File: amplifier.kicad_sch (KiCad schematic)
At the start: 20 parts, among them U5 PAM8403D

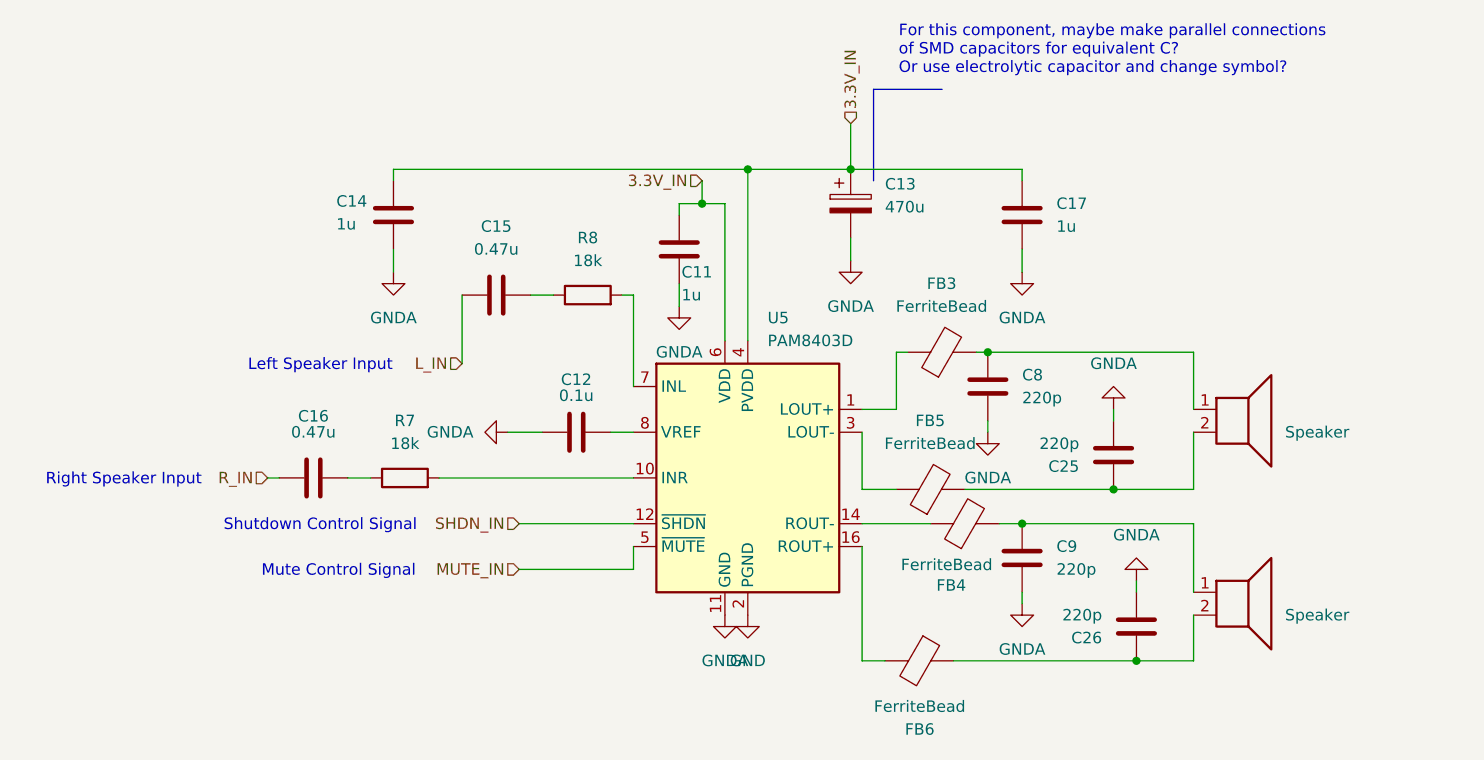
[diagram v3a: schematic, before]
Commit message: Changed grounds and began with new planes
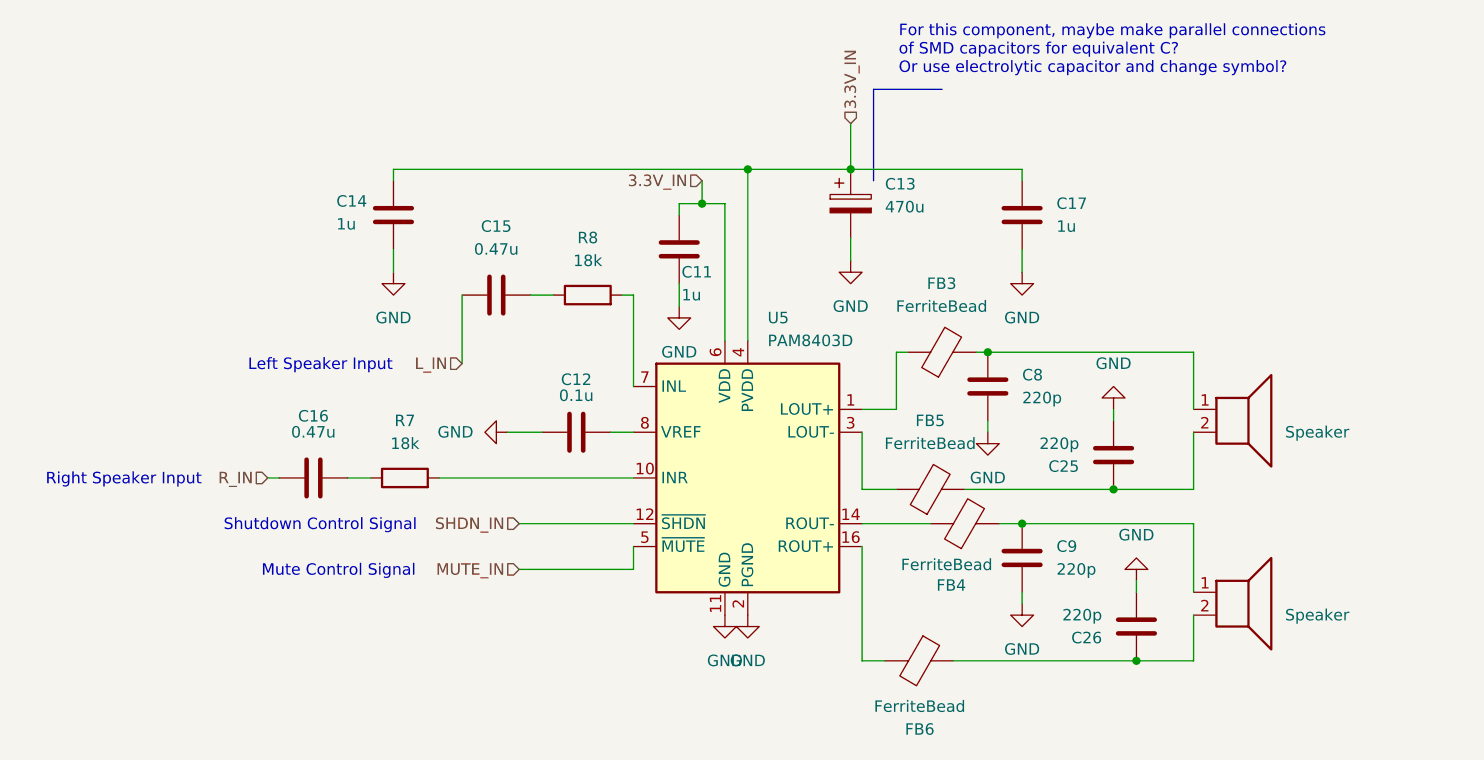
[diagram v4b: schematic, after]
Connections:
- net GNDA is gone; now on net GND: C11.2, C12.1, C13.2, C14.2, C17.2, C25.2, C26.2, C8.2, C9.2, U5.11 (GND)
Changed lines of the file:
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@@
 	)
 	(symbol
-		(lib_id "power:GNDA")
+		(lib_id "power:GND")
 		(at 165.1 106.68 0)
 		(unit 1)
@@
 		(dnp no)
 		(fields_autoplaced yes)
-		(property "Reference" "#PWR034"
+		(property "Reference" "#PWR34"
 			(at 165.1 113.03 0)
 			(effects
@@
 			)
 		)
-		(property "Value" "GNDA"
+		(property "Value" "GND"
 			(at 165.1 111.76 0)
 			(effects
@@
 			)
 		)
-		(property "Description" "Power symbol creates a global label with name \"GNDA\" , analog ground"
+		(property "Description" "Power symbol creates a global label with name \"GND\" , ground"
 			(at 165.1 106.68 0)
 			(effects
@@
 			(project "plant caretaker"
 				(path "/23b35dcc-615e-4aec-abee-c26cc3d8b906/64bd70cc-1431-45fc-8946-041e9631b1bb"
-					(reference "#PWR034")
+					(reference "#PWR34")
 					(unit 1)
 				)
@@
 	)
 	(symbol
-		(lib_id "power:GNDA")
+		(lib_id "power:GND")
 		(at 165.1 69.85 0)
 		(unit 1)
@@
 		(dnp no)
 		(fields_autoplaced yes)
-		(property "Reference" "#PWR033"
+		(property "Reference" "#PWR33"
 			(at 165.1 76.2 0)
 			(effects
@@
 			)
 		)
-		(property "Value" "GNDA"
+		(property "Value" "GND"
 			(at 165.1 74.93 0)
 			(effects
@@
 			)
 		)
-		(property "Description" "Power symbol creates a global label with name \"GNDA\" , analog ground"
+		(property "Description" "Power symbol creates a global label with name \"GND\" , ground"
 			(at 165.1 69.85 0)
 			(effects
@@
 			(project "plant caretaker"
 				(path "/23b35dcc-615e-4aec-abee-c26cc3d8b906/64bd70cc-1431-45fc-8946-041e9631b1bb"
-					(reference "#PWR033")
+					(reference "#PWR33")
 					(unit 1)
 				)
@@
 		(dnp no)
 		(fields_autoplaced yes)
-		(property "Reference" "#PWR011"
+		(property "Reference" "#PWR11"
 			(at 134.62 114.3 0)
 			(effects
@@
 			(project "plant caretaker"
 				(path "/23b35dcc-615e-4aec-abee-c26cc3d8b906/64bd70cc-1431-45fc-8946-041e9631b1bb"
-					(reference "#PWR011")
+					(reference "#PWR11")
 					(unit 1)
 				)
@@
 	)
 	(symbol
-		(lib_id "power:GNDA")
+		(lib_id "power:GND")
 		(at 161.29 87.63 0)
 		(unit 1)
@@
 		(dnp no)
 		(fields_autoplaced yes)
-		(property "Reference" "#PWR035"
+		(property "Reference" "#PWR35"
 			(at 161.29 93.98 0)
 			(effects
@@
 			)
 		)
-		(property "Value" "GNDA"
+		(property "Value" "GND"
 			(at 161.29 92.71 0)
 			(effects
@@
 			)
 		)
-		(property "Description" "Power symbol creates a global label with name \"GNDA\" , analog ground"
+		(property "Description" "Power symbol creates a global label with name \"GND\" , ground"
 			(at 161.29 87.63 0)
 			(effects
@@
 			(project "plant caretaker"
 				(path "/23b35dcc-615e-4aec-abee-c26cc3d8b906/64bd70cc-1431-45fc-8946-041e9631b1bb"
-					(reference "#PWR035")
+					(reference "#PWR35")
 					(unit 1)
 				)
@@
 	)
 	(symbol
-		(lib_id "power:GNDA")
+		(lib_id "power:GND")
 		(at 95.25 69.85 0)
 		(unit 1)
@@
 		(dnp no)
 		(fields_autoplaced yes)
-		(property "Reference" "#PWR012"
+		(property "Reference" "#PWR12"
 			(at 95.25 76.2 0)
 			(effects
@@
 			)
 		)
-		(property "Value" "GNDA"
+		(property "Value" "GND"
 			(at 95.25 74.93 0)
 			(effects
@@
 			)
 		)
-		(property "Description" "Power symbol creates a global label with name \"GNDA\" , analog ground"
+		(property "Description" "Power symbol creates a global label with name \"GND\" , ground"
 			(at 95.25 69.85 0)
 			(effects
@@
 			(project "plant caretaker"
 				(path "/23b35dcc-615e-4aec-abee-c26cc3d8b906/64bd70cc-1431-45fc-8946-041e9631b1bb"
-					(reference "#PWR012")
-					(unit 1)
-				)
-			)
-		)
-	)
-	(symbol
-		(lib_id "power:GNDA")
+					(reference "#PWR12")
+					(unit 1)
+				)
+			)
+		)
+	)
+	(symbol
+		(lib_id "power:GND")
 		(at 175.26 85.09 180)
 		(unit 1)
@@
 		(dnp no)
 		(fields_autoplaced yes)
-		(property "Reference" "#PWR038"
+		(property "Reference" "#PWR38"
 			(at 175.26 78.74 0)
 			(effects
@@
 			)
 		)
-		(property "Value" "GNDA"
+		(property "Value" "GND"
 			(at 175.26 80.01 0)
 			(effects
@@
 			)
 		)
-		(property "Description" "Power symbol creates a global label with name \"GNDA\" , analog ground"
+		(property "Description" "Power symbol creates a global label with name \"GND\" , ground"
 			(at 175.26 85.09 0)
 			(effects
@@
 			(project "plant caretaker"
 				(path "/23b35dcc-615e-4aec-abee-c26cc3d8b906/64bd70cc-1431-45fc-8946-041e9631b1bb"
-					(reference "#PWR038")
+					(reference "#PWR38")
 					(unit 1)
 				)
@@
 	)
 	(symbol
-		(lib_id "power:GNDA")
+		(lib_id "power:GND")
 		(at 107.95 87.63 270)
 		(unit 1)
@@
 		(dnp no)
 		(fields_autoplaced yes)
-		(property "Reference" "#PWR013"
+		(property "Reference" "#PWR13"
 			(at 101.6 87.63 0)
 			(effects
@@
 			)
 		)
-		(property "Value" "GNDA"
+		(property "Value" "GND"
 			(at 104.14 87.6299 90)
 			(effects
@@
 			)
 		)
-		(property "Description" "Power symbol creates a global label with name \"GNDA\" , analog ground"
+		(property "Description" "Power symbol creates a global label with name \"GND\" , ground"
 			(at 107.95 87.63 0)
 			(effects
@@
 			(project "plant caretaker"
 				(path "/23b35dcc-615e-4aec-abee-c26cc3d8b906/64bd70cc-1431-45fc-8946-041e9631b1bb"
-					(reference "#PWR013")
-					(unit 1)
-				)
-			)
-		)
-	)
-	(symbol
-		(lib_id "power:GNDA")
+					(reference "#PWR13")
+					(unit 1)
+				)
+			)
+		)
+	)
+	(symbol
+		(lib_id "power:GND")
 		(at 127 73.66 0)
 		(unit 1)
@@
 		(dnp no)
 		(fields_autoplaced yes)
-		(property "Reference" "#PWR014"
+		(property "Reference" "#PWR14"
 			(at 127 80.01 0)
 			(effects
@@
 			)
 		)
-		(property "Value" "GNDA"
+		(property "Value" "GND"
 			(at 127 78.74 0)
 			(effects
@@
 			)
 		)
-		(property "Description" "Power symbol creates a global label with name \"GNDA\" , analog ground"
+		(property "Description" "Power symbol creates a global label with name \"GND\" , ground"
 			(at 127 73.66 0)
 			(effects
@@
 			(project "plant caretaker"
 				(path "/23b35dcc-615e-4aec-abee-c26cc3d8b906/64bd70cc-1431-45fc-8946-041e9631b1bb"
-					(reference "#PWR014")
+					(reference "#PWR14")
 					(unit 1)
 				)
@@
 	)
 	(symbol
-		(lib_id "power:GNDA")
+		(lib_id "power:GND")
 		(at 177.8 104.14 180)
 		(unit 1)
@@
 		(dnp no)
 		(fields_autoplaced yes)
-		(property "Reference" "#PWR041"
+		(property "Reference" "#PWR41"
 			(at 177.8 97.79 0)
 			(effects
@@
 			)
 		)
-		(property "Value" "GNDA"
+		(property "Value" "GND"
 			(at 177.8 99.06 0)
 			(effects
@@
 			)
 		)
-		(property "Description" "Power symbol creates a global label with name \"GNDA\" , analog ground"
+		(property "Description" "Power symbol creates a global label with name \"GND\" , ground"
 			(at 177.8 104.14 0)
 			(effects
@@
 			(project "plant caretaker"
 				(path "/23b35dcc-615e-4aec-abee-c26cc3d8b906/64bd70cc-1431-45fc-8946-041e9631b1bb"
-					(reference "#PWR041")
+					(reference "#PWR41")
 					(unit 1)
 				)
@@
 	)
 	(symbol
-		(lib_id "power:GNDA")
+		(lib_id "power:GND")
 		(at 132.08 107.95 0)
 		(unit 1)
@@
 		(dnp no)
 		(fields_autoplaced yes)
-		(property "Reference" "#PWR015"
+		(property "Reference" "#PWR15"
 			(at 132.08 114.3 0)
 			(effects
@@
 			)
 		)
-		(property "Value" "GNDA"
+		(property "Value" "GND"
 			(at 132.08 113.03 0)
 			(effects
@@
 			)
 		)
-		(property "Description" "Power symbol creates a global label with name \"GNDA\" , analog ground"
+		(property "Description" "Power symbol creates a global label with name \"GND\" , ground"
 			(at 132.08 107.95 0)
 			(effects
@@
 			(project "plant caretaker"
 				(path "/23b35dcc-615e-4aec-abee-c26cc3d8b906/64bd70cc-1431-45fc-8946-041e9631b1bb"
-					(reference "#PWR015")
+					(reference "#PWR15")
 					(unit 1)
 				)
@@
 	)
 	(symbol
-		(lib_id "power:GNDA")
+		(lib_id "power:GND")
 		(at 146.05 68.58 0)
 		(unit 1)
@@
 		(dnp no)
 		(fields_autoplaced yes)
-		(property "Reference" "#PWR09"
+		(property "Reference" "#PWR9"
 			(at 146.05 74.93 0)
 			(effects
@@
 			)
 		)
-		(property "Value" "GNDA"
+		(property "Value" "GND"
 			(at 146.05 73.66 0)
 			(effects
@@
 			)
 		)
-		(property "Description" "Power symbol creates a global label with name \"GNDA\" , analog ground"
+		(property "Description" "Power symbol creates a global label with name \"GND\" , ground"
 			(at 146.05 68.58 0)
 			(effects
@@
 			(project "plant caretaker"
 				(path "/23b35dcc-615e-4aec-abee-c26cc3d8b906/64bd70cc-1431-45fc-8946-041e9631b1bb"
-					(reference "#PWR09")
-					(unit 1)
-				)
+					(reference "#PWR9")
+					(unit 1)
+				)

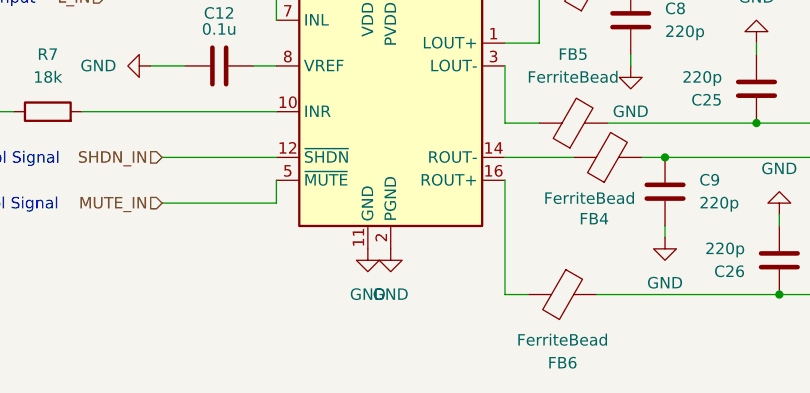
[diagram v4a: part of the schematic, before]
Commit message: Finished with ground planes and made board smaller
WARNING: Unconnected "ground power" for audio amplifier

Also fixed the ESP32 footprint on board only
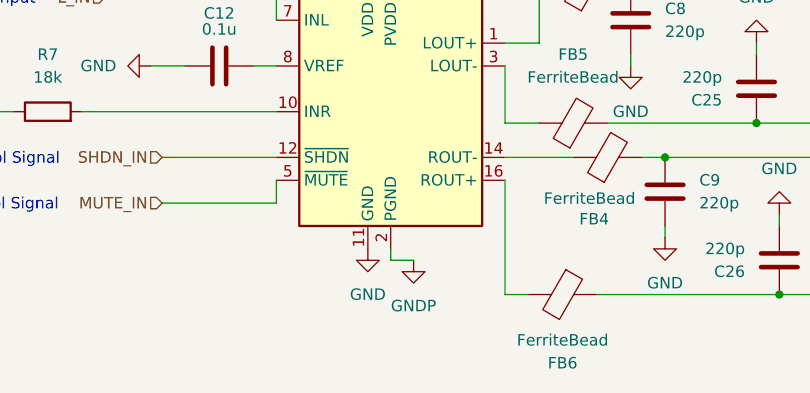
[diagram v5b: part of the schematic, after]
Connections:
- net GND: no longer U5.15 (PGND), U5.2 (PGND)
- new net GNDP: U5.15 (PGND), U5.2 (PGND)
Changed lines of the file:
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@@
+	(wire
+		(pts
+			(xy 134.62 109.22) (xy 134.62 107.95)
+		)
+		(stroke
+			(width 0)
+			(type default)
+		)
+	)
 	(wire
 		(pts
@@
 		(pts
 			(xy 175.26 93.98) (xy 184.15 93.98)
+		)
+		(stroke
+			(width 0)
+			(type default)
+		)
+	)
+	(wire
+		(pts
+			(xy 137.16 109.22) (xy 134.62 109.22)
 		)
 		(stroke
@@
 		(dnp no)
 		(fields_autoplaced yes)
-		(property "Reference" "#PWR34"
+		(property "Reference" "#PWR034"
 			(at 165.1 113.03 0)
 			(effects
@@
 			(project "plant caretaker"
 				(path "/23b35dcc-615e-4aec-abee-c26cc3d8b906/64bd70cc-1431-45fc-8946-041e9631b1bb"
-					(reference "#PWR34")
+					(reference "#PWR034")
 					(unit 1)
 				)
@@
 		(dnp no)
 		(fields_autoplaced yes)
-		(property "Reference" "#PWR33"
+		(property "Reference" "#PWR033"
 			(at 165.1 76.2 0)
 			(effects
@@
 			(project "plant caretaker"
 				(path "/23b35dcc-615e-4aec-abee-c26cc3d8b906/64bd70cc-1431-45fc-8946-041e9631b1bb"
-					(reference "#PWR33")
-					(unit 1)
-				)
-			)
-		)
-	)
-	(symbol
-		(lib_id "power:GND")
-		(at 134.62 107.95 0)
-		(unit 1)
-		(exclude_from_sim no)
-		(in_bom yes)
-		(on_board yes)
-		(dnp no)
-		(fields_autoplaced yes)
-		(property "Reference" "#PWR11"
-			(at 134.62 114.3 0)
-			(effects
-				(font
-					(size 1.27 1.27)
-				)
-				(hide yes)
-			)
-		)
-		(property "Value" "GND"
-			(at 134.62 113.03 0)
-			(effects
-				(font
-					(size 1.27 1.27)
-				)
-			)
-		)
-		(property "Footprint" ""
-			(at 134.62 107.95 0)
-			(effects
-				(font
-					(size 1.27 1.27)
-				)
-				(hide yes)
-			)
-		)
-		(property "Datasheet" ""
-			(at 134.62 107.95 0)
-			(effects
-				(font
-					(size 1.27 1.27)
-				)
-				(hide yes)
-			)
-		)
-		(property "Description" "Power symbol creates a global label with name \"GND\" , ground"
-			(at 134.62 107.95 0)
-			(effects
-				(font
-					(size 1.27 1.27)
-				)
-				(hide yes)
-			)
-		)
-		(pin "1"
-		)
-		(instances
-			(project "plant caretaker"
-				(path "/23b35dcc-615e-4aec-abee-c26cc3d8b906/64bd70cc-1431-45fc-8946-041e9631b1bb"
-					(reference "#PWR11")
+					(reference "#PWR033")
 					(unit 1)
 				)
@@
 		(dnp no)
 		(fields_autoplaced yes)
-		(property "Reference" "#PWR35"
+		(property "Reference" "#PWR035"
 			(at 161.29 93.98 0)
 			(effects
@@
 			(project "plant caretaker"
 				(path "/23b35dcc-615e-4aec-abee-c26cc3d8b906/64bd70cc-1431-45fc-8946-041e9631b1bb"
-					(reference "#PWR35")
+					(reference "#PWR035")
+					(unit 1)
+				)
+			)
+		)
+	)
+	(symbol
+		(lib_id "power:GND")
+		(at 137.16 109.22 0)
+		(unit 1)
+		(exclude_from_sim no)
+		(in_bom yes)
+		(on_board yes)
+		(dnp no)
+		(fields_autoplaced yes)
+		(property "Reference" "#PWR011"
+			(at 137.16 115.57 0)
+			(effects
+				(font
+					(size 1.27 1.27)
+				)
+				(hide yes)
+			)
+		)
+		(property "Value" "GNDP"
+			(at 137.16 114.3 0)
+			(effects
+				(font
+					(size 1.27 1.27)
+				)
+			)
+		)
+		(property "Footprint" ""
+			(at 137.16 109.22 0)
+			(effects
+				(font
+					(size 1.27 1.27)
+				)
+				(hide yes)
+			)
+		)
+		(property "Datasheet" ""
+			(at 137.16 109.22 0)
+			(effects
+				(font
+					(size 1.27 1.27)
+				)
+				(hide yes)
+			)
+		)
+		(property "Description" "Power symbol creates a global label with name \"GND\" , ground"
+			(at 137.16 109.22 0)
+			(effects
+				(font
+					(size 1.27 1.27)
+				)
+				(hide yes)
+			)
+		)
+		(pin "1"
+		)
+		(instances
+			(project "plant caretaker"
+				(path "/23b35dcc-615e-4aec-abee-c26cc3d8b906/64bd70cc-1431-45fc-8946-041e9631b1bb"
+					(reference "#PWR011")
 					(unit 1)
 				)
@@
 		(dnp no)
 		(fields_autoplaced yes)
-		(property "Reference" "#PWR12"
+		(property "Reference" "#PWR012"
 			(at 95.25 76.2 0)
 			(effects
@@
 			(project "plant caretaker"
 				(path "/23b35dcc-615e-4aec-abee-c26cc3d8b906/64bd70cc-1431-45fc-8946-041e9631b1bb"
-					(reference "#PWR12")
+					(reference "#PWR012")
 					(unit 1)
 				)
@@
 		(dnp no)
 		(fields_autoplaced yes)
-		(property "Reference" "#PWR38"
+		(property "Reference" "#PWR038"
 			(at 175.26 78.74 0)
 			(effects
@@
 			(project "plant caretaker"
 				(path "/23b35dcc-615e-4aec-abee-c26cc3d8b906/64bd70cc-1431-45fc-8946-041e9631b1bb"
-					(reference "#PWR38")
+					(reference "#PWR038")
 					(unit 1)
 				)
@@
 		(dnp no)
 		(fields_autoplaced yes)
-		(property "Reference" "#PWR13"
+		(property "Reference" "#PWR013"
 			(at 101.6 87.63 0)
 			(effects
@@
 			(project "plant caretaker"
 				(path "/23b35dcc-615e-4aec-abee-c26cc3d8b906/64bd70cc-1431-45fc-8946-041e9631b1bb"
-					(reference "#PWR13")
+					(reference "#PWR013")
 					(unit 1)
 				)
@@
 		(dnp no)
 		(fields_autoplaced yes)
-		(property "Reference" "#PWR14"
+		(property "Reference" "#PWR014"
 			(at 127 80.01 0)
 			(effects
@@
 			(project "plant caretaker"
 				(path "/23b35dcc-615e-4aec-abee-c26cc3d8b906/64bd70cc-1431-45fc-8946-041e9631b1bb"
-					(reference "#PWR14")
+					(reference "#PWR014")
 					(unit 1)
 				)
@@
 		(dnp no)
 		(fields_autoplaced yes)
-		(property "Reference" "#PWR41"
+		(property "Reference" "#PWR041"
 			(at 177.8 97.79 0)
 			(effects
@@
 			(project "plant caretaker"
 				(path "/23b35dcc-615e-4aec-abee-c26cc3d8b906/64bd70cc-1431-45fc-8946-041e9631b1bb"
-					(reference "#PWR41")
+					(reference "#PWR041")
 					(unit 1)
 				)
@@
 		(dnp no)
 		(fields_autoplaced yes)
-		(property "Reference" "#PWR15"
+		(property "Reference" "#PWR015"
 			(at 132.08 114.3 0)
 			(effects
@@
 			(project "plant caretaker"
 				(path "/23b35dcc-615e-4aec-abee-c26cc3d8b906/64bd70cc-1431-45fc-8946-041e9631b1bb"
-					(reference "#PWR15")
+					(reference "#PWR015")
 					(unit 1)
 				)
@@
 		(dnp no)
 		(fields_autoplaced yes)
-		(property "Reference" "#PWR9"
+		(property "Reference" "#PWR09"
 			(at 146.05 74.93 0)
 			(effects
@@
 			(project "plant caretaker"
 				(path "/23b35dcc-615e-4aec-abee-c26cc3d8b906/64bd70cc-1431-45fc-8946-041e9631b1bb"
-					(reference "#PWR9")
-					(unit 1)
-				)
+					(reference "#PWR09")
+					(unit 1)
+				)
